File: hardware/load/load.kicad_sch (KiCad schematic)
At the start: 10 parts, among them J101 vin_kelvin, J102 uart, J103 panel, J105 vin, J106 dut, J107 fan, J108 fuse 20A

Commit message: feat(load): route logic and optmize layout
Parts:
- added J104: external_trigger, TerminalBlock:TerminalBlock_bornier-3_P5.08mm, symbol Connector_Generic:Conn_01x03
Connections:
- net GND: now also J104.3 (Pin_3)
- new net stm32/external_trigger_in: J104.2 (Pin_2)
- new net stm32/external_trigger_out: J104.1 (Pin_1)
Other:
- sheet stm32 ports: added external_trigger_in, external_trigger_out; removed none
- moved on the sheet: D101, J101, J102, J103, J105, J106, J107, J108, R101, R102

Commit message: feat(load): finzalize power routing and add mounting holes
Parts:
- added H101, H102, H103, H104, H105, H106, H107, H108, H109, H110: MountingHole, MountingHole:MountingHole_3.2mm_M3, symbol Mechanical:MountingHole
- J105: value vin -> input; footprint Connector_PinHeader_2.54mm:PinHeader_1x02_P2.54mm_Vertical -> TerminalBlock:TerminalBlock_bornier-2_P5.08mm
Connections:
- net GND: now also J105.1 (Pin_1); no longer J105.2 (Pin_2)
- net supplies/input: now also J105.2 (Pin_2); no longer J105.1 (Pin_1)

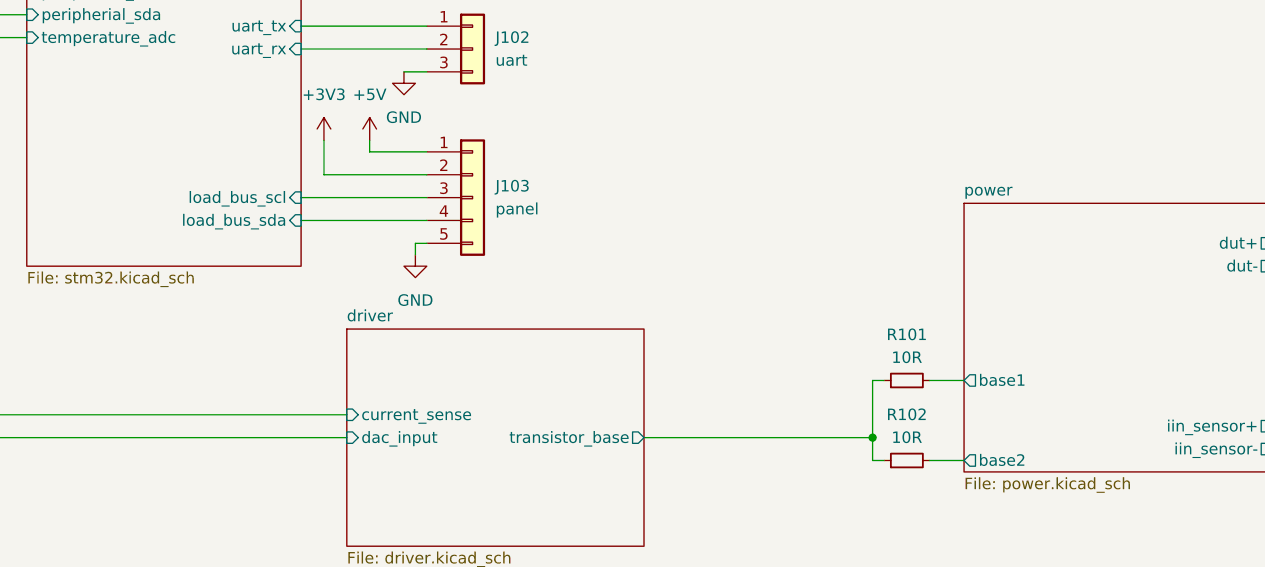
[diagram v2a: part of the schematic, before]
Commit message: feat(load): modify analog PID values on the schematic
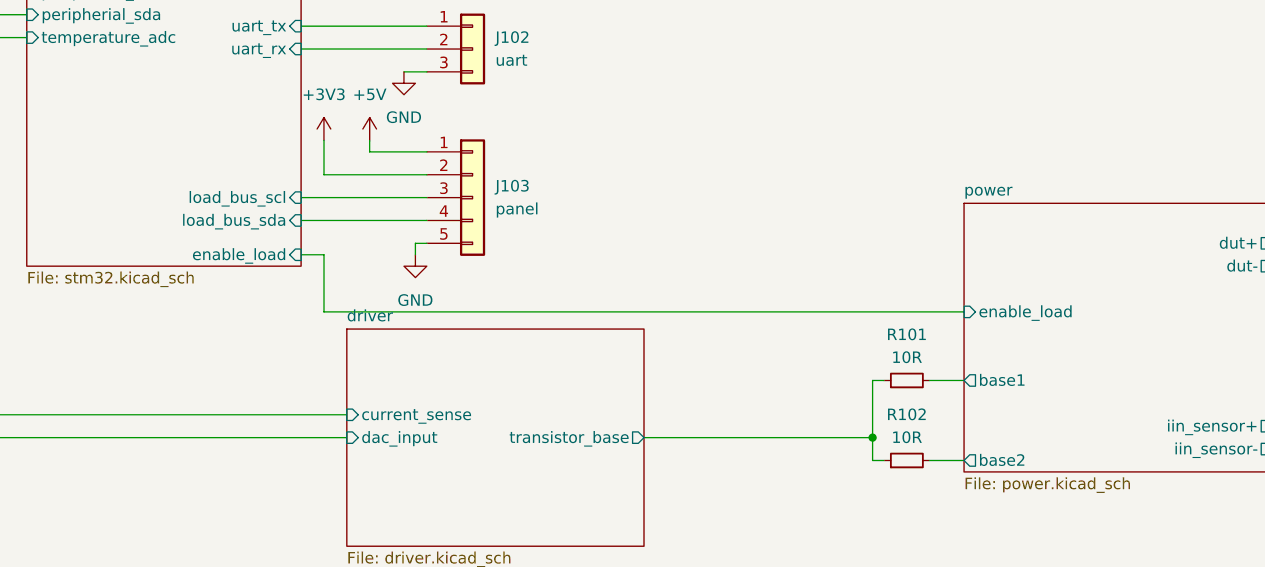
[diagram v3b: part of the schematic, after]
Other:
- sheet power ports: added enable_load; removed none
- sheet stm32 ports: added enable_load; removed none
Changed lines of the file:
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@@
+	(wire
+		(pts
+			(xy 200.66 111.76) (xy 129.54 111.76)
+		)
+		(stroke
+			(width 0)
+			(type default)
+		)
+	)
 	(wire
 		(pts
@@
 	(wire
 		(pts
+			(xy 129.54 111.76) (xy 129.54 105.41)
+		)
+		(stroke
+			(width 0)
+			(type default)
+		)
+	)
+	(wire
+		(pts
 			(xy 190.5 125.73) (xy 190.5 128.27)
 		)
@@
 		(pts
 			(xy 184.15 35.56) (xy 184.15 38.1)
+		)
+		(stroke
+			(width 0)
+			(type default)
+		)
+	)
+	(wire
+		(pts
+			(xy 127 105.41) (xy 129.54 105.41)
 		)
 		(stroke
@@
 			)
 		)
+		(pin "enable_load" input
+			(at 200.66 111.76 180)
+			(effects
+				(font
+					(size 1.27 1.27)
+				)
+				(justify left)
+			)
+		)
 		(instances
 			(project "load"
@@
 			(effects
 				(font
+					(size 1.27 1.27)
+				)
+				(justify right)
+			)
+		)
+		(pin "enable_load" input
+			(at 127 105.41 0)
+			(effects
+				(font
